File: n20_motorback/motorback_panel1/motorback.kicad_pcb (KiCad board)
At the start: 2 copper layers, 21.4 x 11 mm, 13 parts, among them J1 Servo wire input, J2 Conn_01x01_Male, J3 Conn_01x01_Male, U1 DRV8837DSGR, U2 ATtiny13V-10SSU, U3 AIC1734-33GUTR

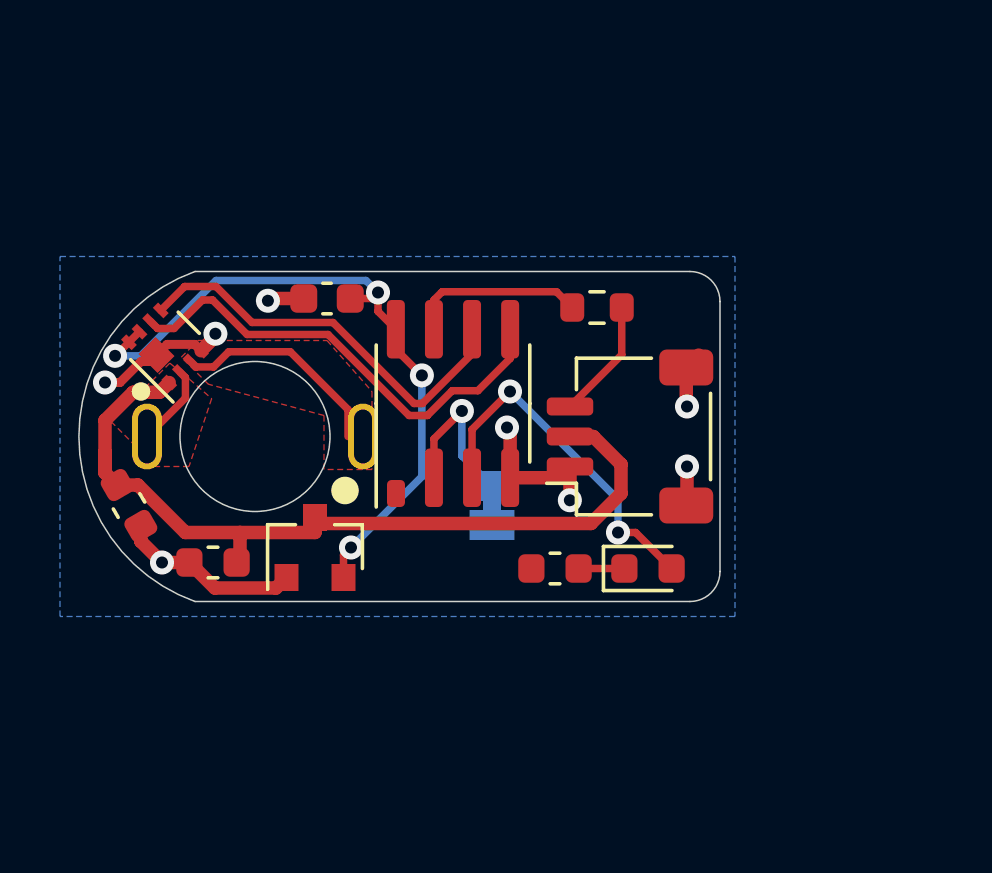
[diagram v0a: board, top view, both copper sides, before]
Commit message: mod soic8 footprint, minor updates
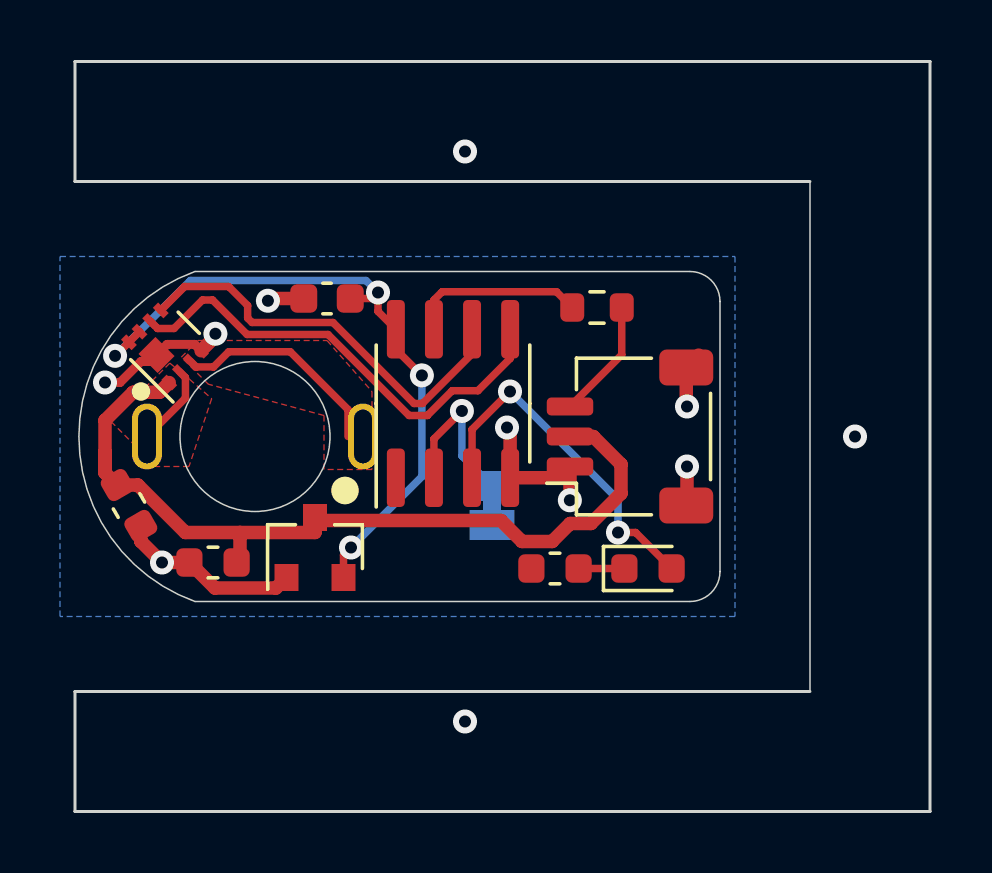
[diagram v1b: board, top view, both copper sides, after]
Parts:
- U2: footprint motorback:SOIC-8_shortpin1 -> Package_SO:SOIC-8_3.9x4.9mm_P1.27mm
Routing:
- net (no net): vias 0 -> 3
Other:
- board size 21.4 x 11 mm -> 28.5 x 25 mm
- board text removed: "@markxr 2021"

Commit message: panel resync
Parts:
- U2: footprint Package_SO:SOIC-8_3.9x4.9mm_P1.27mm -> motorback:SOIC-8_shortpin1
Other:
- board text added: "@markxr 2021"
